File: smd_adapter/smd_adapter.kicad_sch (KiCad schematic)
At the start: 6 parts, among them J1 Conn_01x01_Pin, J2 Conn_01x01_Pin, J3 Conn_01x01_Pin, J4 Conn_01x01_Pin, J5 Conn_01x01_Pin, U2 MCP73831-5-OT

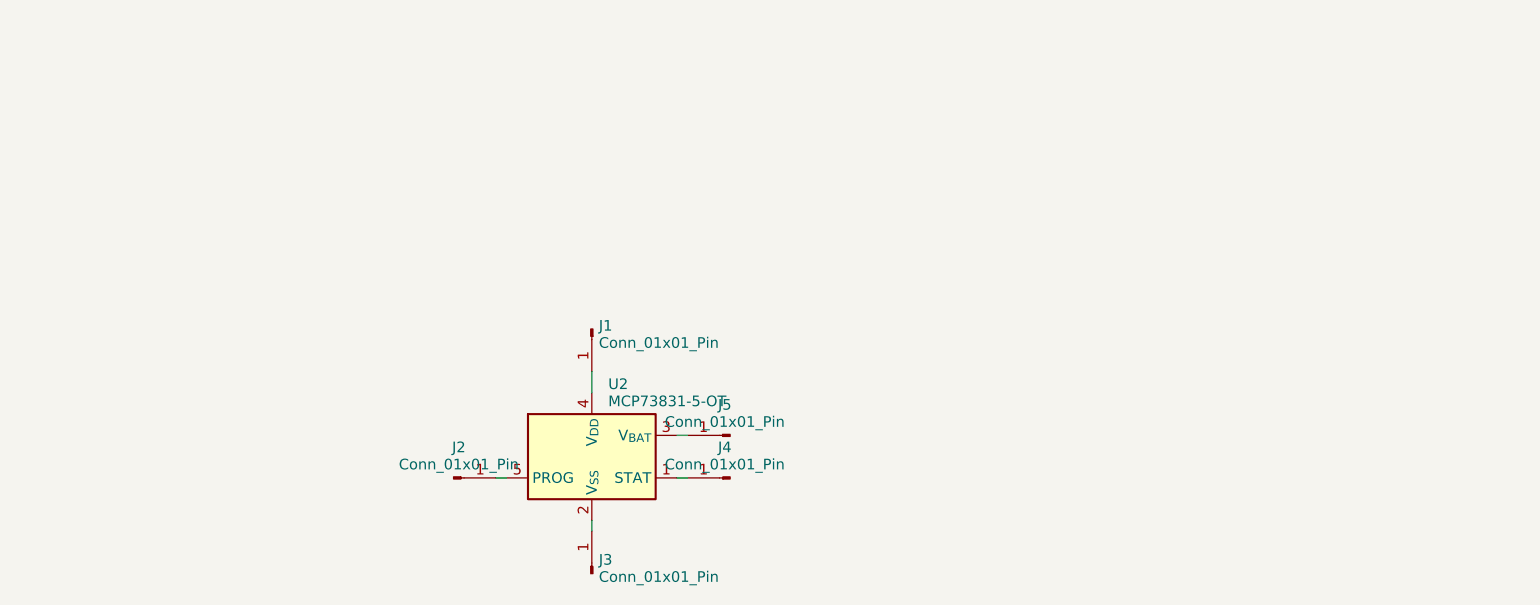
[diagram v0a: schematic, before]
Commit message: Completed the layout of the smd adapters (5 kinds)
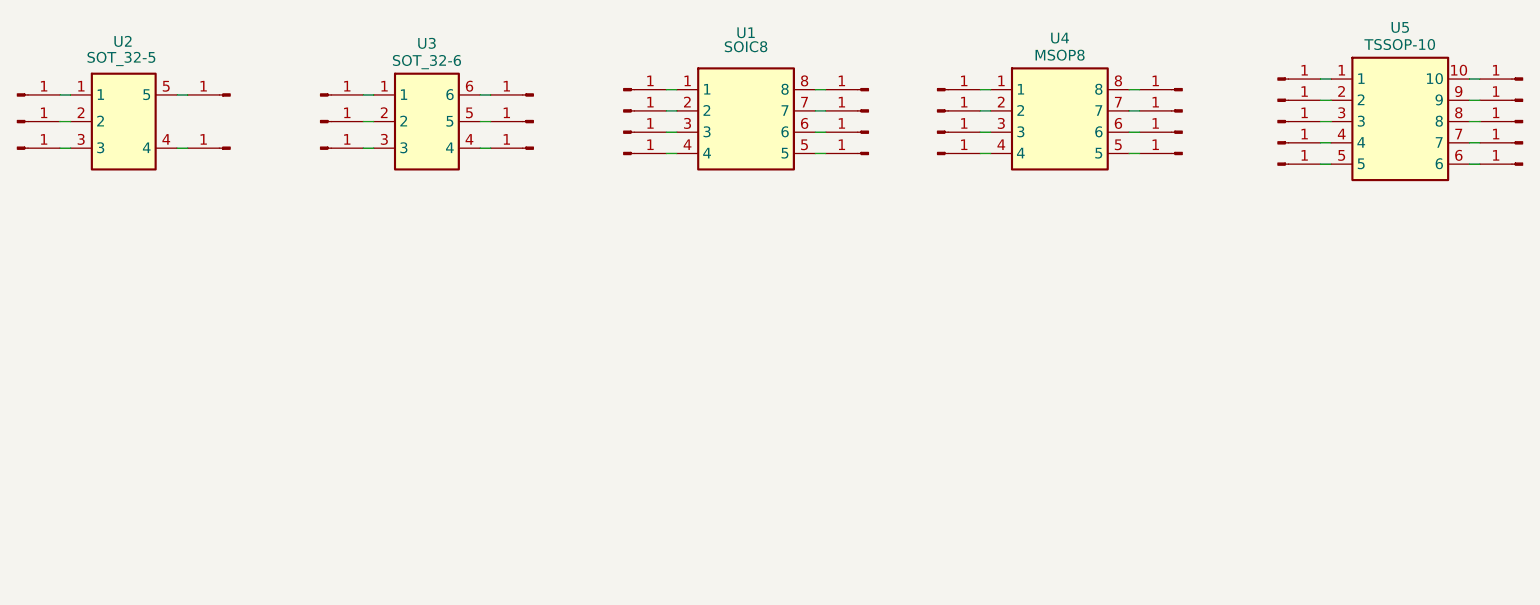
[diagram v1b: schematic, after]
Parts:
- added J10, J11, J12, J13, J14, J15, J16, J17, J18, J19, J20, J21, J22, J23, J24, J25, J26, J27, J28, J29, J30, J31, J32, J33, J34, J35, J36, J37, J6, J7, J8, J9: Conn_01x01_Pin, smd_adapter:pin_pad, symbol Connector:Conn_01x01_Pin
- added U1: SOIC8, smd_adapter:SOIC8, symbol smd_adapter:SOIC8
- added U3: SOT_32-6, smd_adapter:SOT-23-6, symbol smd_adapter:SOT_32-6
- added U4: MSOP8, smd_adapter:MSOP-8, symbol smd_adapter:MSOP8
- added U5: TSSOP-10, smd_adapter:TSSOP-10, symbol smd_adapter:TSSOP-10
- U2: value MCP73831-5-OT -> SOT_32-5; symbol Battery_Management:MCP73831-5-OT -> smd_adapter:SOT_32-5
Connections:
- new net: J11.1 (Pin_1), U1.7
- new net: J20.1 (Pin_1), U4.1
- new net: J21.1 (Pin_1), U4.2
- new net: J22.1 (Pin_1), U4.3
- new net: J23.1 (Pin_1), U4.4
- new net: J27.1 (Pin_1), U4.5
- new net: J26.1 (Pin_1), U4.6
- new net: J25.1 (Pin_1), U4.7
- new net: J24.1 (Pin_1), U4.8
- new net: J29.1 (Pin_1), U5.2
- new net: J13.1 (Pin_1), U1.5
- new net: J10.1 (Pin_1), U1.8
- new net: J6.1 (Pin_1), U1.1
- new net: J7.1 (Pin_1), U1.2
- new net: J8.1 (Pin_1), U1.3
- new net: J9.1 (Pin_1), U1.4
- new net: J12.1 (Pin_1), U1.6
- new net: J30.1 (Pin_1), U5.3
- new net: J33.1 (Pin_1), U5.10
- new net: J28.1 (Pin_1), U5.1
- new net: J31.1 (Pin_1), U5.4
- new net: J32.1 (Pin_1), U5.5
- new net: J37.1 (Pin_1), U5.6
- new net: J36.1 (Pin_1), U5.7
- new net: J35.1 (Pin_1), U5.8
- new net: J34.1 (Pin_1), U5.9
- new net: J16.1 (Pin_1), U3.3
- new net: J18.1 (Pin_1), U3.5
- new net: J19.1 (Pin_1), U3.4
- new net: J17.1 (Pin_1), U3.6
- new net: J14.1 (Pin_1), U3.1
- new net: J15.1 (Pin_1), U3.2
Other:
- title: (none) -> SMD ADAPTERS  V0.1
- moved on the sheet: U2
